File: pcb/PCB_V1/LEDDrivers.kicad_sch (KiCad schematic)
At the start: 50 parts, among them J711 LED +/- (return isolated), J721 LED +/- (return isolated), J731 LED +/- (return isolated), Q711 CSD19534Q5A, Q721 CSD19538Q3A, U700 SN74LVC1G08DBVR, U710 AL8853S-13, U720 AL8853S-13

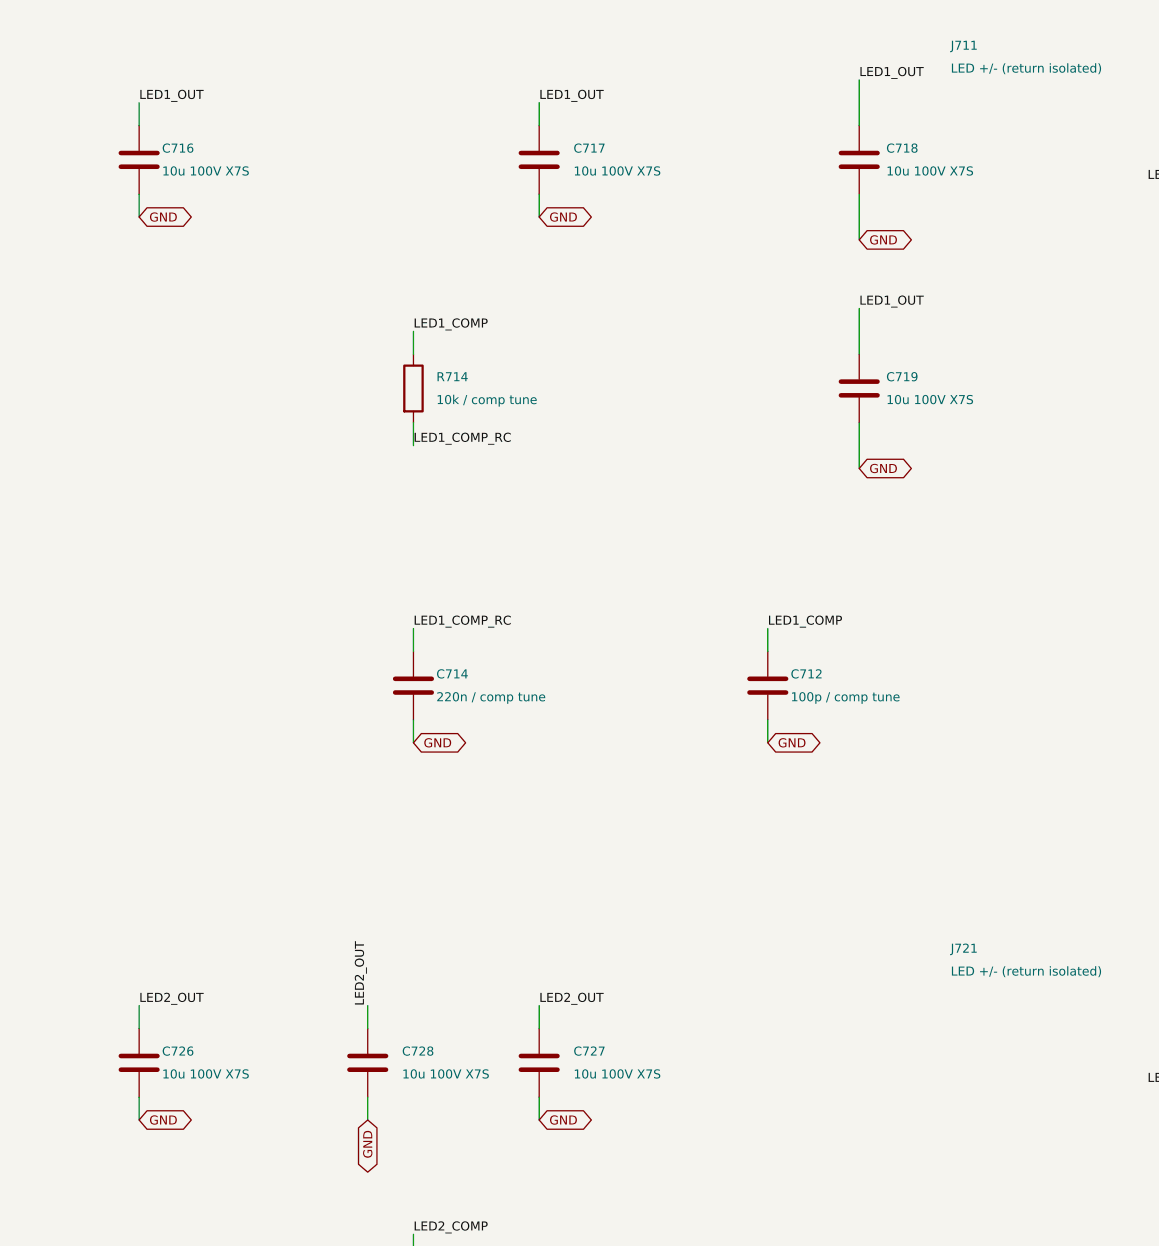
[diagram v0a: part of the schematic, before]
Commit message: pcb: revision 0.19 cost-down in the schematic, same footprints
Schematic and calculations only; PCB_V1.kicad_pcb is untouched on the
user's request. All substitutions keep footprints and nets.

- C716-C719, C726-C728: TDK C3225X7R2A106K250AC (X7R, published DC-bias
  curve 2.35 uF at 49 V) instead of Samsung CL32Y106KCV6PNE.
- C104/C105/C401: Samsung CL21A226MPQNNNE X5R; C521/C710/C715/C725/
  C905/C906: Taiyo Yuden UMK325AB7106KMHP.
- C602 shares CL21A106KAYNNNE with C201 (1.41 uF screen >= 1 uF);
  D601 shares SMBJ26CA with D901 (D_TVS symbol, 42.1 V clamp);
  R501/R511/R521 33R; F904 3 A shared with F721.
- analyze_led_power/analyze_power_path/verify_netlist updated; price and
  JLC snapshots v19; reports, sheet images and checks log v19.
- COST_DOWN.md: USD 37.50 per board (was 39.82), 65 purchase codes,
  rejected candidates and board status.

verify_board.py reports value differences for 17 parts until the board
is synced (footprints and nets already match); all other checks pass.

Co-Authored-By: Claude Opus 5.5 <noreply@anthropic.com>
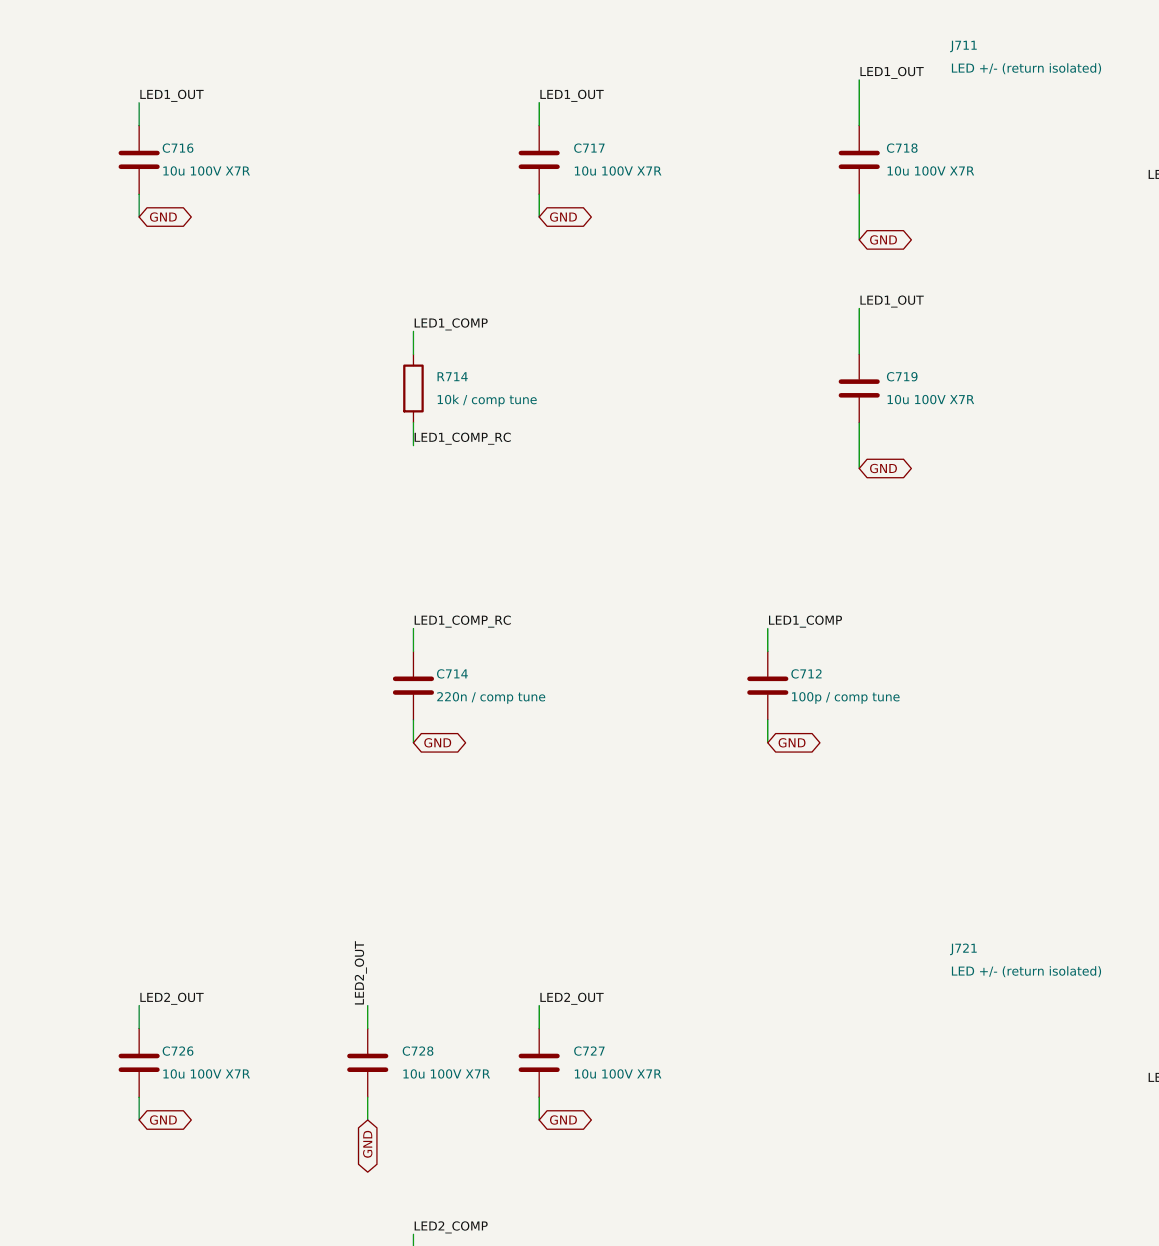
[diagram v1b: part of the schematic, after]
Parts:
- C710, C715, C725: LCSC C77102 -> C386166; MPN GRM32ER71H106KA12L -> UMK325AB7106KMHP; Manufacturer Murata -> Taiyo Yuden
- C716, C717, C718, C719, C726, C727: value 10u 100V X7S -> 10u 100V X7R; LCSC C22380050 -> C49296968; MPN CL32Y106KCV6PNE -> C3225X7R2A106K250AC; Manufacturer Samsung Electro-Mechanics -> TDK
- C728: value 10u 100V X7S -> 10u 100V X7R; LCSC C22380050 -> C49296968; MPN CL32Y106KCV6PNE -> C3225X7R2A106K250AC; Manufacturer Samsung -> TDK
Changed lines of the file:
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@@
 			)
 		)
-		(property "Datasheet" ""
+		(property "Datasheet" "https://ds.yuden.co.jp/TYCOMPAS/ut/detail?pn=UMK325AB7106KMHP"
 			(at 165.1 156.21 0)
 			(hide yes)
@@
 			)
 		)
-		(property "LCSC" "C77102"
+		(property "LCSC" "C386166"
 			(at 165.1 156.21 0)
 			(effects
@@
 			)
 		)
-		(property "MPN" "GRM32ER71H106KA12L"
+		(property "MPN" "UMK325AB7106KMHP"
 			(at 165.1 156.21 0)
 			(effects
@@
 			)
 		)
-		(property "Manufacturer" "Murata"
+		(property "Manufacturer" "Taiyo Yuden"
 			(at 165.1 156.21 0)
 			(effects
@@
 			)
 		)
-		(property "Value" "10u 100V X7S"
+		(property "Value" "10u 100V X7R"
 			(at 322.58 199.39 0)
 			(show_name no)
@@
 			)
 		)
-		(property "Datasheet" "https://product.samsungsem.com/mlcc/CL32Y106KCV6PN.do"
+		(property "Datasheet" "https://product.tdk.com/en/search/capacitor/ceramic/mlcc/info?part_no=C3225X7R2A106K250AC"
 			(at 320.04 198.12 0)
 			(hide yes)
@@
 			)
 		)
-		(property "Manufacturer" "Samsung Electro-Mechanics"
+		(property "Manufacturer" "TDK"
 			(at 320.04 198.12 0)
 			(hide yes)
@@
 			)
 		)
-		(property "MPN" "CL32Y106KCV6PNE"
+		(property "MPN" "C3225X7R2A106K250AC"
 			(at 320.04 198.12 0)
 			(hide yes)
@@
 			)
 		)
-		(property "LCSC" "C22380050"
+		(property "LCSC" "C49296968"
 			(at 320.04 198.12 0)
 			(hide yes)
@@
 			)
 		)
-		(property "Value" "10u 100V X7S"
+		(property "Value" "10u 100V X7R"
 			(at 368.3 199.39 0)
 			(show_name no)
@@
 			)
 		)
-		(property "Datasheet" "https://product.samsungsem.com/mlcc/CL32Y106KCV6PN.do"
+		(property "Datasheet" "https://product.tdk.com/en/search/capacitor/ceramic/mlcc/info?part_no=C3225X7R2A106K250AC"
 			(at 364.49 198.12 0)
 			(hide yes)
@@
 			)
 		)
-		(property "Manufacturer" "Samsung Electro-Mechanics"
+		(property "Manufacturer" "TDK"
 			(at 364.49 198.12 0)
 			(hide yes)
@@
 			)
 		)
-		(property "MPN" "CL32Y106KCV6PNE"
+		(property "MPN" "C3225X7R2A106K250AC"
 			(at 364.49 198.12 0)
 			(hide yes)
@@
 			)
 		)
-		(property "LCSC" "C22380050"
+		(property "LCSC" "C49296968"
 			(at 364.49 198.12 0)
 			(hide yes)
@@
 			)
 		)
-		(property "Value" "10u 100V X7S"
+		(property "Value" "10u 100V X7R"
 			(at 368.3 99.06 0)
 			(show_name no)
@@
 			)
 		)
-		(property "Datasheet" "https://product.samsungsem.com/mlcc/CL32Y106KCV6PN.do"
+		(property "Datasheet" "https://product.tdk.com/en/search/capacitor/ceramic/mlcc/info?part_no=C3225X7R2A106K250AC"
 			(at 364.49 97.79 0)
 			(hide yes)
@@
 			)
 		)
-		(property "Manufacturer" "Samsung Electro-Mechanics"
+		(property "Manufacturer" "TDK"
 			(at 364.49 97.79 0)
 			(hide yes)
@@
 			)
 		)
-		(property "MPN" "CL32Y106KCV6PNE"
+		(property "MPN" "C3225X7R2A106K250AC"
 			(at 364.49 97.79 0)
 			(hide yes)
@@
 			)
 		)
-		(property "LCSC" "C22380050"
+		(property "LCSC" "C49296968"
 			(at 364.49 97.79 0)
 			(hide yes)
@@
 			)
 		)
-		(property "Datasheet" ""
+		(property "Datasheet" "https://ds.yuden.co.jp/TYCOMPAS/ut/detail?pn=UMK325AB7106KMHP"
 			(at 165.1 256.54 0)
 			(hide yes)
@@
 			)
 		)
-		(property "LCSC" "C77102"
+		(property "LCSC" "C386166"
 			(at 165.1 256.54 0)
 			(effects
@@
 			)
 		)
-		(property "MPN" "GRM32ER71H106KA12L"
+		(property "MPN" "UMK325AB7106KMHP"
 			(at 165.1 256.54 0)
 			(effects
@@
 			)
 		)
-		(property "Manufacturer" "Murata"
+		(property "Manufacturer" "Taiyo Yuden"
 			(at 165.1 256.54 0)
 			(effects
@@
 			)
 		)
-		(property "Value" "10u 100V X7S"
+		(property "Value" "10u 100V X7R"
 			(at 322.58 99.06 0)
 			(show_name no)
@@
 			)
 		)
-		(property "Datasheet" "https://product.samsungsem.com/mlcc/CL32Y106KCV6PN.do"
+		(property "Datasheet" "https://product.tdk.com/en/search/capacitor/ceramic/mlcc/info?part_no=C3225X7R2A106K250AC"
 			(at 320.04 97.79 0)
 			(hide yes)
@@
 			)
 		)
-		(property "Manufacturer" "Samsung Electro-Mechanics"
+		(property "Manufacturer" "TDK"
 			(at 320.04 97.79 0)
 			(hide yes)
@@
 			)
 		)
-		(property "MPN" "CL32Y106KCV6PNE"
+		(property "MPN" "C3225X7R2A106K250AC"
 			(at 320.04 97.79 0)
 			(hide yes)
@@
 			)
 		)
-		(property "LCSC" "C22380050"
+		(property "LCSC" "C49296968"
 			(at 320.04 97.79 0)
 			(hide yes)
@@
 			)
 		)
-		(property "Value" "10u 100V X7S"
+		(property "Value" "10u 100V X7R"
 			(at 403.05 99.06 0)
 			(effects
@@
 			)
 		)
-		(property "Datasheet" "https://product.samsungsem.com/mlcc/CL32Y106KCV6PN.do"
+		(property "Datasheet" "https://product.tdk.com/en/search/capacitor/ceramic/mlcc/info?part_no=C3225X7R2A106K250AC"
 			(at 400.05 97.79 0)
 			(effects
@@
 			)
 		)
-		(property "Manufacturer" "Samsung Electro-Mechanics"
+		(property "Manufacturer" "TDK"
 			(at 400.05 97.79 0)
 			(effects
@@
 			)
 		)
-		(property "MPN" "CL32Y106KCV6PNE"
+		(property "MPN" "C3225X7R2A106K250AC"
 			(at 400.05 97.79 0)
 			(effects
@@
 			)
 		)
-		(property "LCSC" "C22380050"
+		(property "LCSC" "C49296968"
 			(at 400.05 97.79 0)
 			(effects
@@
 			)
 		)
-		(property "Value" "10u 100V X7S"
+		(property "Value" "10u 100V X7R"
 			(at 403.05 124.46 0)
 			(effects
@@
 			)
 		)
-		(property "Datasheet" "https://product.samsungsem.com/mlcc/CL32Y106KCV6PN.do"
+		(property "Datasheet" "https://product.tdk.com/en/search/capacitor/ceramic/mlcc/info?part_no=C3225X7R2A106K250AC"
 			(at 400.05 123.19 0)
 			(effects
@@
 			)
 		)
-		(property "Manufacturer" "Samsung Electro-Mechanics"
+		(property "Manufacturer" "TDK"
 			(at 400.05 123.19 0)
 			(effects
@@
 			)
 		)
-		(property "MPN" "CL32Y106KCV6PNE"
+		(property "MPN" "C3225X7R2A106K250AC"
 			(at 400.05 123.19 0)
 			(effects
@@
 			)
 		)
-		(property "LCSC" "C22380050"
+		(property "LCSC" "C49296968"
 			(at 400.05 123.19 0)
 			(effects
@@
 			)
 		)
-		(property "Datasheet" ""
+		(property "Datasheet" "https://ds.yuden.co.jp/TYCOMPAS/ut/detail?pn=UMK325AB7106KMHP"
 			(at 40.64 148.59 0)
 			(effects
@@
 			)
 		)
-		(property "Manufacturer" "Murata"
+		(property "Manufacturer" "Taiyo Yuden"
 			(at 40.64 148.59 0)
 			(effects
@@
 			)
 		)
-		(property "MPN" "GRM32ER71H106KA12L"
+		(property "MPN" "UMK325AB7106KMHP"
 			(at 40.64 148.59 0)
 			(effects
@@
 			)
 		)
-		(property "LCSC" "C77102"
+		(property "LCSC" "C386166"
 			(at 40.64 148.59 0)
 			(effects
@@
 			)
 		)
-		(property "Value" "10u 100V X7S"
+		(property "Value" "10u 100V X7R"
 			(at 349.25 199.39 0)
 			(effects
@@
 			)
 		)
-		(property "Datasheet" ""
+		(property "Datasheet" "https://product.tdk.com/en/search/capacitor/ceramic/mlcc/info?part_no=C3225X7R2A106K250AC"
 			(at 345.44 198.12 0)
 			(effects
@@
 			)
 		)
-		(property "Manufacturer" "Samsung"
+		(property "Manufacturer" "TDK"
 			(at 345.44 198.12 0)
 			(effects
@@
 			)
 		)
-		(property "MPN" "CL32Y106KCV6PNE"
+		(property "MPN" "C3225X7R2A106K250AC"
 			(at 345.44 198.12 0)
 			(effects
@@
 			)
 		)
-		(property "LCSC" "C22380050"
+		(property "LCSC" "C49296968"
 			(at 345.44 198.12 0)
 			(effects
